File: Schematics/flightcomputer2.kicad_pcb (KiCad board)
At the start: 4 copper layers, 50 x 100 mm, 80 parts, among them J1 Microsemi_FlashPro-JTAG-10, J2 Pyro, J3 USB_C_Receptacle, J4 Conn_Coaxial_Small, J4 Pyro, J5 Conn_01x05_Pin, J6 Conn_01x05_Pin, J7 Conn_Coaxial_Small, J8 Micro_SD_Card, Q1 BSC098N10NS5, Q2 BSC098N10NS5, U1 STM32F405RGT6, U2 SN65HVD230, U3 LDL1117-3.3, U4 RFM95W-915S2, U5 MPL3115A2R1, U6 LSM6DS3TR-C, U7 H3LIS100DL, U8 W25Q128JVP, Y1 8mhz

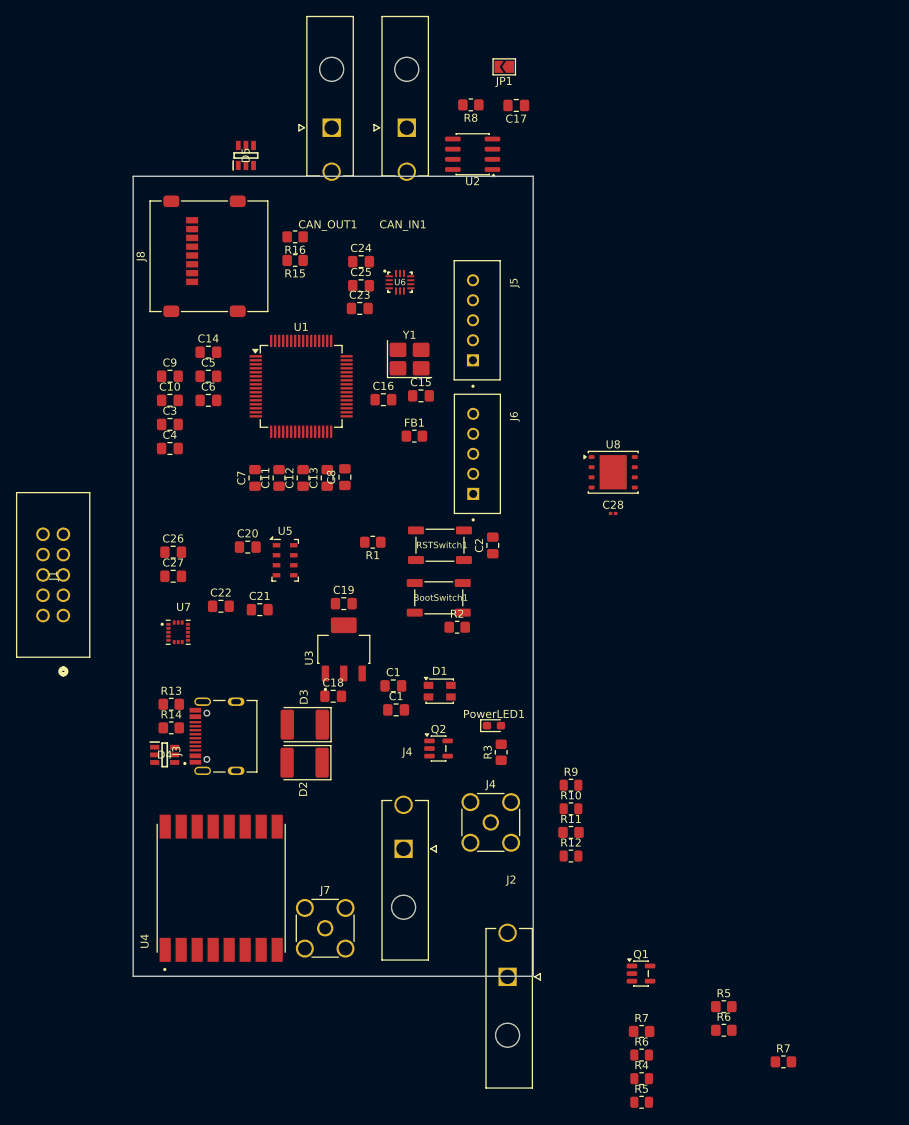
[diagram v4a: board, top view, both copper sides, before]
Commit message: first layout need to go over schematic
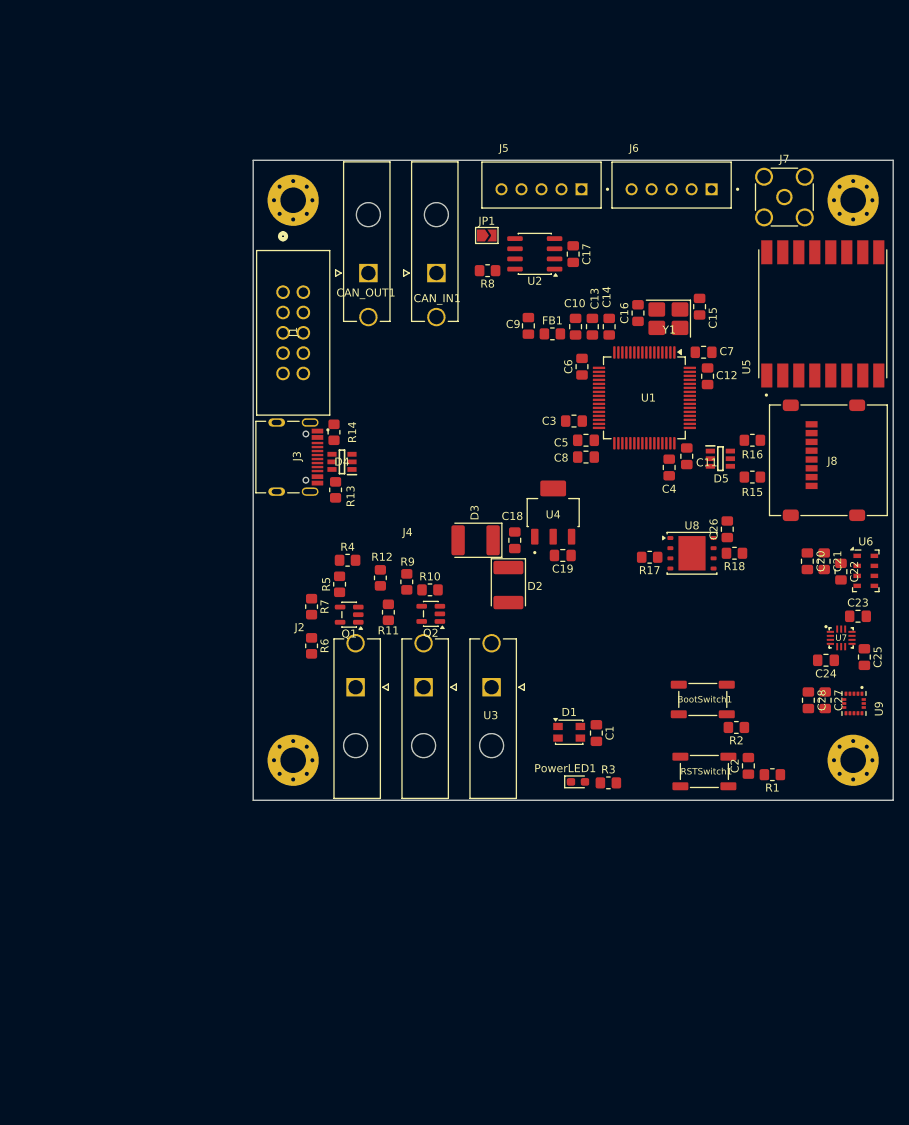
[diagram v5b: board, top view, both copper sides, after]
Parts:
- removed the C1 at (132.9, 116.7)
- removed the J4 at (144.7, 130.8)
- removed the R5 at (173.8, 153.8)
- removed the R6 at (173.8, 156.8)
- removed the R7 at (163.6, 156.9)
- added R17: 10k, Resistor_SMD:R_0805_2012Metric_Pad1.20x1.40mm_HandSolder, F.Cu at (164.6, 97.6)
- added R18: 10k, Resistor_SMD:R_0805_2012Metric_Pad1.20x1.40mm_HandSolder, F.Cu at (175.2, 97.1)
- added REF**: MountingHole_3.2mm_M3_Pad_Via, MountingHole:MountingHole_3.2mm_M3_Pad_Via, F.Cu at (190.0, 123.0)
- added REF**: MountingHole_3.2mm_M3_Pad_Via, MountingHole:MountingHole_3.2mm_M3_Pad_Via, F.Cu at (120.0, 53.0)
- added REF**: MountingHole_3.2mm_M3_Pad_Via, MountingHole:MountingHole_3.2mm_M3_Pad_Via, F.Cu at (190.0, 53.0)
- added REF**: MountingHole_3.2mm_M3_Pad_Via, MountingHole:MountingHole_3.2mm_M3_Pad_Via, F.Cu at (120.0, 123.0)
- added U9: H3LIS100DL, myFootprints:PQFN50P300X300X100-16N, F.Cu at (190.1, 115.9)
- C27: value 1u -> 100nf
- C28: value 100nF -> 1u; footprint Capacitor_SMD:C_0201_0603Metric -> Capacitor_SMD:C_0805_2012Metric_Pad1.18x1.45mm_HandSolder
- R10, R12, R4, R5, R6, R9: footprint Resistor_SMD:R_0805_2012Metric -> Resistor_SMD:R_0805_2012Metric_Pad1.20x1.40mm_HandSolder
- R7: value 22 -> 15k
- U3: value LDL1117-3.3 -> PowerIn; footprint myFootprints:SOT230P700X180-4N -> myFootprints:MOLEX_26013114
- U4: value RFM95W-915S2 -> LDL1117-3.3; footprint myFootprints:XCVR_RFM95W-915S2 -> myFootprints:SOT230P700X180-4N
- U5: value MPL3115A2R1 -> RFM95W-915S2; footprint Package_LGA:LGA-8_3x5mm_P1.25mm -> myFootprints:XCVR_RFM95W-915S2
- U6: value LSM6DS3TR-C -> MPL3115A2R1; footprint myFootprints:LGA-14-2.5X3MM -> Package_LGA:LGA-8_3x5mm_P1.25mm
- U7: value H3LIS100DL -> LSM6DS3TR-C; footprint myFootprints:PQFN50P300X300X100-16N -> myFootprints:LGA-14-2.5X3MM
- moved J7 107.9 mm to (181.4, 52.6)
- moved C27 83.0 mm to (186.5, 115.5), turned to -90 degrees
- moved U7 82.9 mm to (188.5, 107.7)
- moved R7 82.0 mm to (122.3, 103.8), turned to -90 degrees
- moved J8 81.5 mm to (186.9, 85.5)
- moved C25 78.2 mm to (191.4, 110.1), turned to -90 degrees
- moved C22 77.6 mm to (188.5, 99.4), turned to -90 degrees
- moved C24 76.5 mm to (186.6, 110.5), turned to 180 degrees
- moved R5 75.0 mm to (125.8, 101.0), turned to 90 degrees
- moved R4 74.5 mm to (126.8, 98.0)
- moved U5 73.9 mm to (186.2, 67.2), turned to 90 degrees
- moved C23 73.2 mm to (190.6, 105.0)
- moved C21 70.8 mm to (186.4, 98.1), turned to -90 degrees
- moved D5 70.4 mm to (173.4, 85.3), turned to 0 degrees
- moved C20 70.0 mm to (184.3, 98.1), turned to -90 degrees
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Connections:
- C22 pad 1: Net-(U5-CAP) -> Net-(U6-CAP)
- C26 pad 1: GND -> +3.3V
- C26 pad 2: +3.3V -> GND
- C28 pad 1: +3.3V -> GND
- C28 pad 2: GND -> +3.3V
- J6 pad 2: +3.3V -> GND
- J6 pad 3: GPS2_TX -> /GPS/GPS2_TX
- J6 pad 4: GPS2_RX -> /GPS/GPS2_RX
- J6 pad 5: RESET -> /GPS/RESET2
- R7 pad 1: Net-(J3-Pin_4) -> GND
- R7 pad 2: GPS1_RX -> /MCU/PyroADC
- U3 pad 1: Net-(D2-K) -> +BATT
- U4 pad 1: GND -> Net-(D2-K)
- U4 pad 2: /LoRa/sxMIS0 -> GND
- U4 pad 3: /LoRa/sxMOSI -> +3.3V
- U4 pad 4: /LoRa/sxSCK -> +3.3V
- U5 pad 1: +3.3V -> GND
- U5 pad 2: Net-(U5-CAP) -> /LoRa/sxMIS0
- U5 pad 3: GND -> /LoRa/sxMOSI
- U5 pad 4: +3.3V -> /LoRa/sxSCK
- U5 pad 5: unconnected-(U5-INT2-Pad5) -> /LoRa/sxNSS
- U5 pad 6: unconnected-(U5-INT1-Pad6) -> /LoRa/sxReset
- U5 pad 7: /Accelerometer/AccelerometerSDA -> unconnected-(U5-DIO5-Pad7)
- U5 pad 8: /Accelerometer/AccelerometerSCL -> GND
- U6 pad 1: GND -> +3.3V
- U6 pad 2: GND -> Net-(U6-CAP)
- U6 pad 4: unconnected-(U6-INT1-Pad4) -> +3.3V
- U6 pad 5: +3.3V -> unconnected-(U6-INT2-Pad5)
- U6 pad 6: GND -> unconnected-(U6-INT1-Pad6)
- U6 pad 7: GND -> /Accelerometer/AccelerometerSDA
- U6 pad 8: +3.3V -> /Accelerometer/AccelerometerSCL
- U7 pad 1: +3.3V -> GND
- U7 pad 12: GND -> +3.3V
- U7 pad 13: (no net) -> /Accelerometer/AccelerometerSCL
- U7 pad 14: +3.3V -> /Accelerometer/AccelerometerSDA
- U7 pad 2: unconnected-(U7-NC-Pad2) -> GND
- U7 pad 3: unconnected-(U7-NC-Pad3) -> GND
- U7 pad 4: /Accelerometer/AccelerometerSCL -> unconnected-(U7-INT1-Pad4)
- U7 pad 5: GND -> +3.3V
- U7 pad 6: /Accelerometer/AccelerometerSDA -> GND
- U7 pad 7: unconnected-(U7-SDO/SA0-Pad7) -> GND
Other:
- board size 50 x 100 mm -> 80 x 80 mm

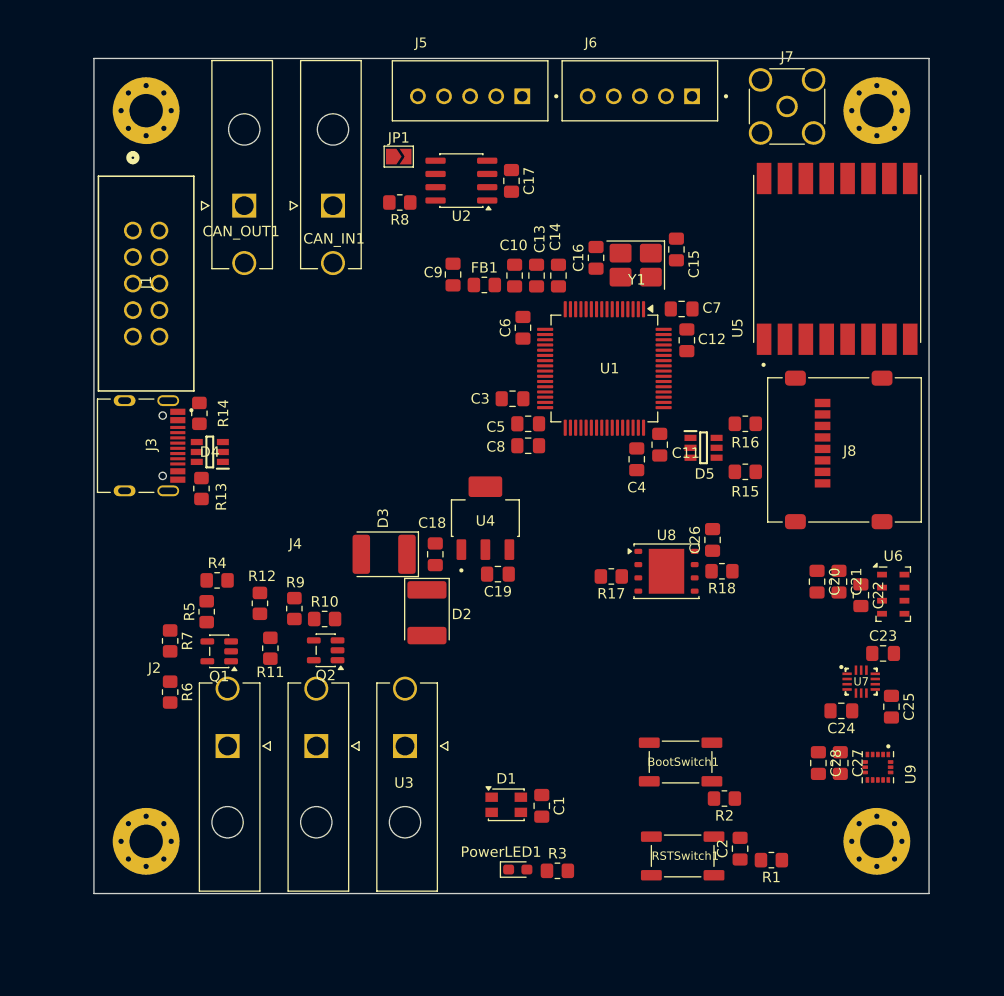
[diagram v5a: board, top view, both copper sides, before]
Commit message: began routing, need layout approval
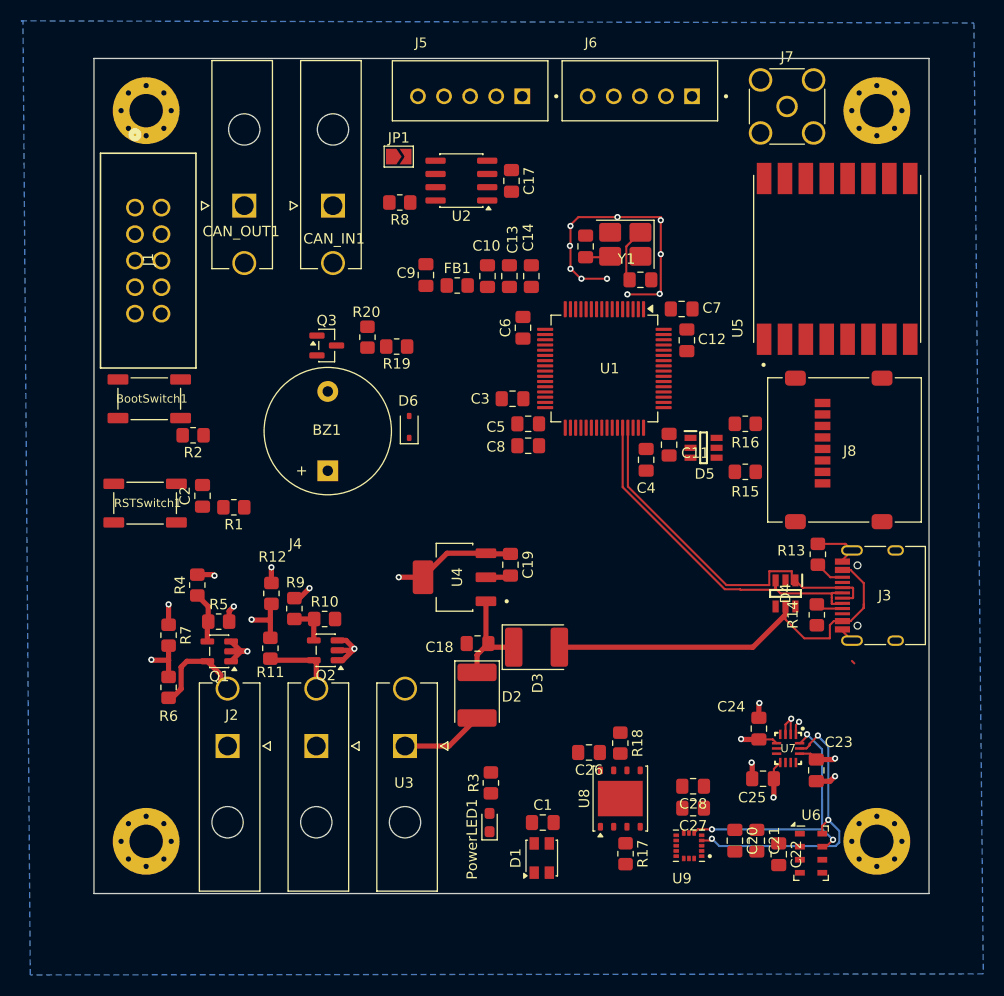
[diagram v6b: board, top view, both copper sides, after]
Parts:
- added BZ1: Buzzer, Buzzer_Beeper:Buzzer_12x9.5RM7.6, F.Cu at (137.4, 87.5)
- added D6: 1N5819WS, Diode_SMD:D_SOD-323, F.Cu at (145.2, 83.3)
- added Q3: BC817, Package_TO_SOT_SMD:SOT-23, F.Cu at (137.3, 75.5)
- added R19: 470r, Resistor_SMD:R_0805_2012Metric_Pad1.20x1.40mm_HandSolder, F.Cu at (144.0, 75.6)
- added R20: 10k, Resistor_SMD:R_0805_2012Metric_Pad1.20x1.40mm_HandSolder, F.Cu at (141.2, 74.7)
- J3: footprint Library:HRO_TYPE-C-31-M-12 -> Connector_USB:USB_C_Receptacle_HRO_TYPE-C-31-M-12
- R11: value 15k -> 75k
- R12: value 10k -> 47k
- R6: value 10k -> 75k
- R7: value 15k -> 47k
- moved J3 74.2 mm to (190.8, 99.5), turned to 90 degrees
- moved R14 62.2 mm to (184.2, 101.3), turned to -90 degrees
- moved R2 61.7 mm to (124.5, 84.1)
- moved BootSwitch1 61.7 mm to (120.3, 80.6)
- moved C2 61.6 mm to (125.4, 89.9)
- moved R1 61.6 mm to (128.4, 91.0)
- moved RSTSwitch1 61.6 mm to (119.9, 90.6)
- moved R13 59.4 mm to (184.3, 95.5), turned to 90 degrees
- moved D4 56.8 mm to (181.2, 99.2), turned to -90 degrees
- moved R17 26.6 mm to (165.9, 124.2), turned to -90 degrees
- moved C20 26.0 mm to (176.4, 122.9)
- moved C21 26.0 mm to (178.5, 122.9)
- moved C22 26.0 mm to (180.6, 124.2)
- moved U6 26.0 mm to (183.7, 124.1)
- moved C26 23.6 mm to (162.4, 114.5), turned to 180 degrees
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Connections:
- U1 pad 16: unconnected-(U1-PA2-Pad16) -> /MCU/BuzzerControl
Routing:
- net GND: track 0.00 -> 62.5 mm, vias 0 -> 20
- net +5V: track 0.00 -> 40.5 mm
- net /MCU/D+: track 0.00 -> 36.1 mm
- net /MCU/D-: track 0.00 -> 34.7 mm
- net /Accelerometer/AccelerometerSDA: track 0.00 -> 28.9 mm, vias 0 -> 3
- net /Accelerometer/AccelerometerSCL: track 0.00 -> 28.7 mm, vias 0 -> 3
- net +3.3V: track 0.00 -> 22.5 mm, vias 0 -> 4
- net Net-(J2-Pin_2): track 0.00 -> 9.96 mm
- net Net-(D2-K): track 0.00 -> 9.93 mm
- net +BATT: track 0.00 -> 8.01 mm
- net Net-(J4-Pin_2): track 0.00 -> 7.04 mm
- net /MCU/OSC IN: track 0.00 -> 5.24 mm
- net /Drogue/DrougeADC: track 0.00 -> 5.11 mm, vias 0 -> 1
- net Net-(Q1-G): track 0.00 -> 4.81 mm
- net /MCU/PyroADC: track 0.00 -> 4.67 mm, vias 0 -> 1
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- added copper zone on In2.Cu, net +3.3V
- added copper zone on B.Cu, net GND
- added copper zone on In1.Cu, net GND

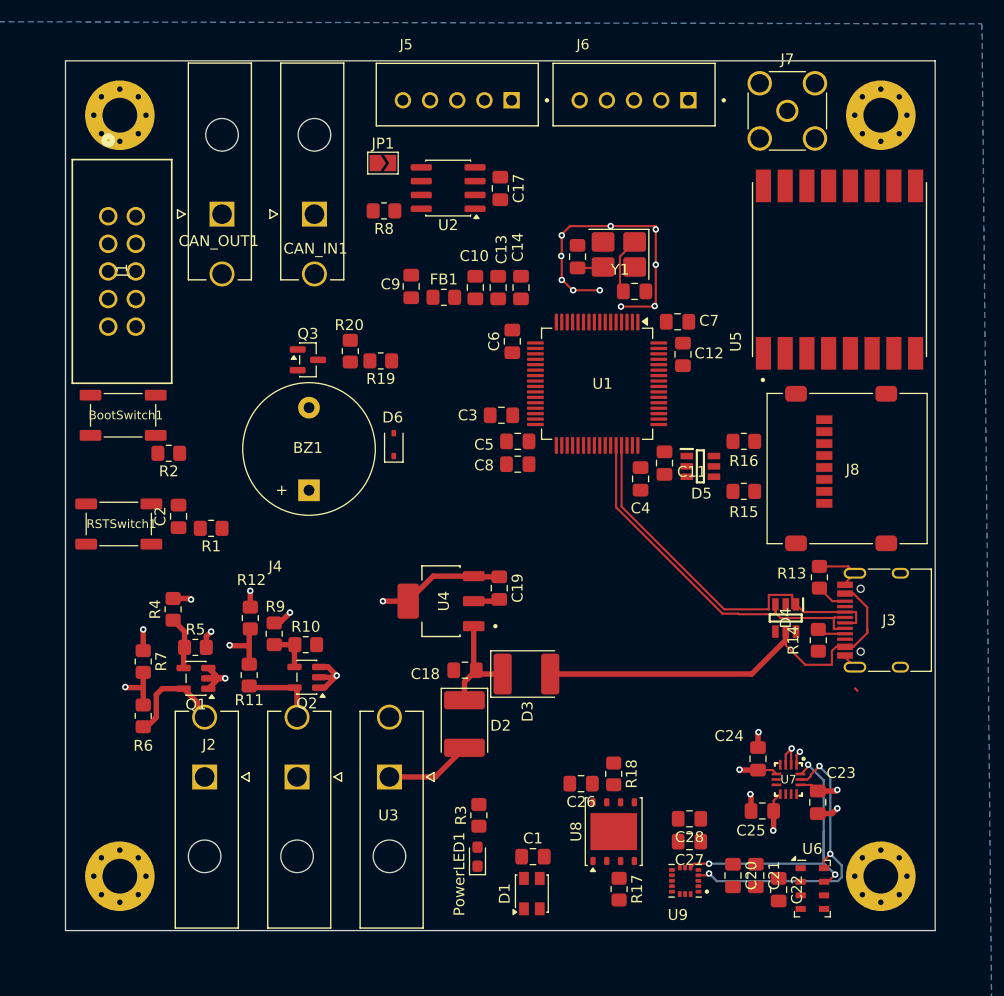
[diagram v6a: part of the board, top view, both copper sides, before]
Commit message: finalizing layout/making it look nice
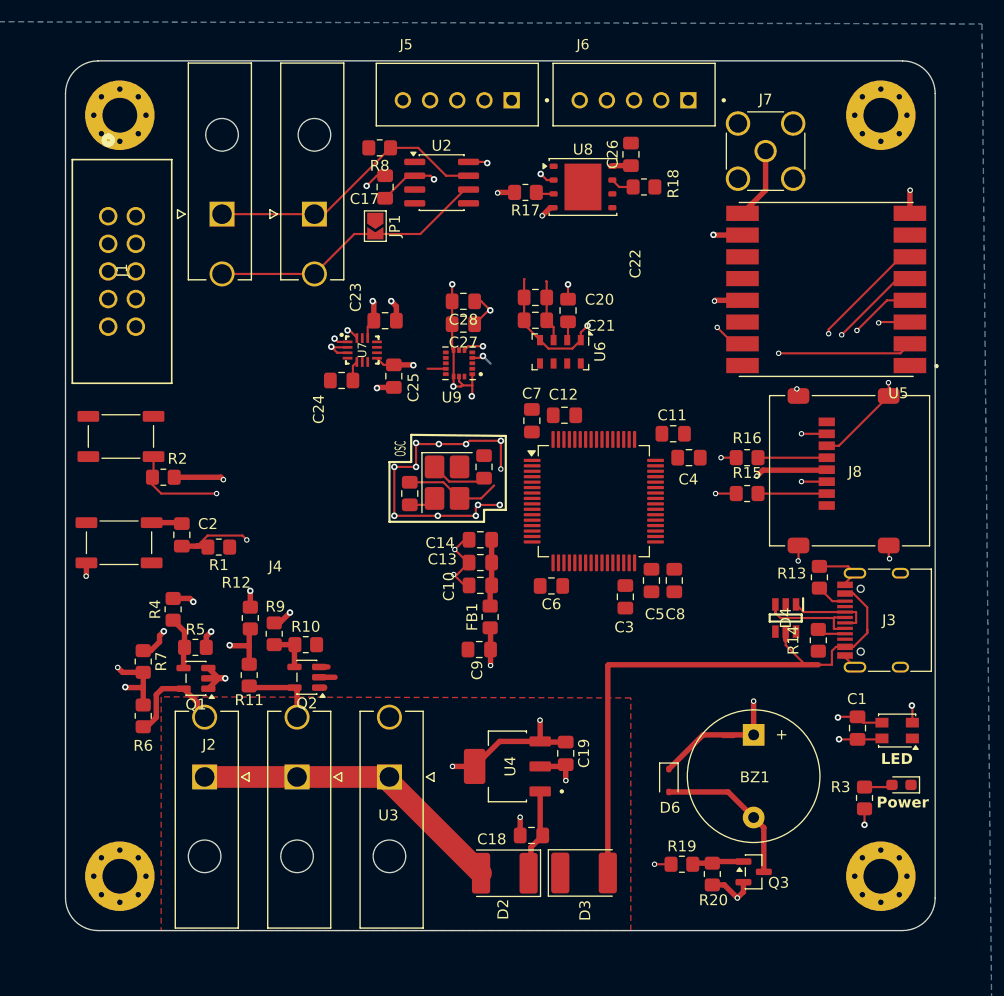
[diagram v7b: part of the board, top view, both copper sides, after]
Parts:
- removed D5: SRV05-4.TCT, myFootprints:SOT95P280X145-6N
- moved R17 64.7 mm to (157.3, 60.1), turned to 180 degrees
- moved Q3 62.4 mm to (178.3, 122.6)
- moved C23 59.6 mm to (144.4, 71.9), turned to 0 degrees
- moved U8 59.4 mm to (162.6, 59.6), turned to 0 degrees
- moved R20 58.5 mm to (174.5, 122.8), turned to 90 degrees
- moved C26 58.1 mm to (167.0, 56.6), turned to 90 degrees
- moved C22 56.7 mm to (161.2, 71.0), turned to 90 degrees
- moved C20 56.2 mm to (158.2, 69.8), turned to 0 degrees
- moved U7 55.6 mm to (142.3, 74.6), turned to 0 degrees
- moved C21 55.0 mm to (158.2, 71.9), turned to 0 degrees
- moved U6 54.5 mm to (160.5, 74.8), turned to -90 degrees
- moved R18 54.1 mm to (168.2, 59.6), turned to 0 degrees
- moved R19 54.0 mm to (171.7, 121.9), turned to 0 degrees
- moved C25 52.4 mm to (145.2, 77.0), turned to -90 degrees
- moved U9 51.9 mm to (151.2, 75.8)
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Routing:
- net +3.3V: track 22.5 -> 88.3 mm, vias 4 -> 17
- net GND: track 62.5 -> 127.7 mm, vias 20 -> 39
- net /MCU/D+: track 36.1 -> 7.79 mm
- net /Accelerometer/AccelerometerSCL: track 28.7 -> 2.04 mm, vias 3 -> 1
- net /Can_transceiver/CANH: track 0.00 -> 26.3 mm
- net /Accelerometer/AccelerometerSDA: track 28.9 -> 3.03 mm, vias 3 -> 2
- net /Can_transceiver/CANL: track 0.00 -> 25.9 mm
- net /MCU/D-: track 34.7 -> 10.2 mm
- net +BATT: track 8.01 -> 29.3 mm
- net +5V: track 40.5 -> 56.0 mm
- net Net-(BZ1--): track 0.00 -> 14.2 mm
- net /LoRa/sxMIS0: track 0.00 -> 12.4 mm, vias 0 -> 1
- net /LoRa/sxReset: track 0.00 -> 10.6 mm, vias 0 -> 1
- net /MCU/BOOT0: track 0.00 -> 8.87 mm, vias 0 -> 1
- net /LoRa/sxNSS: track 0.00 -> 8.42 mm, vias 0 -> 1
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- added copper zone on F.Cu, net (none)
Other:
- outline, holes or cut-outs redrawn
- board text added: "LED"
- board text added: "OSC"
- board text added: "Power"
